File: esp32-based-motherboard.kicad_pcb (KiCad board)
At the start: 2 copper layers, 4 parts, among them J1 HR911105A, U1 ESP32-P4_MODULE, U2 LAN8720A, U3 ADM3053

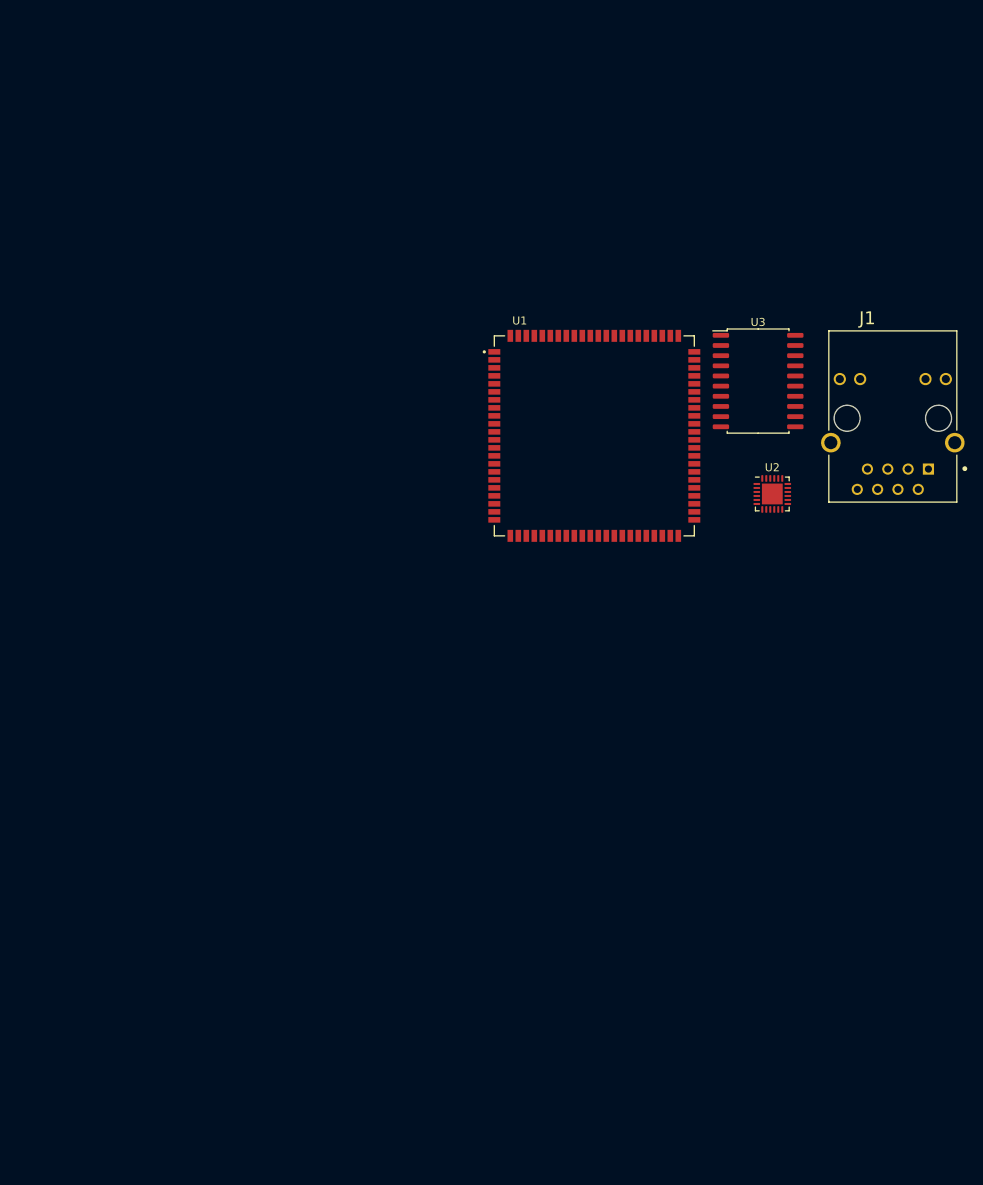
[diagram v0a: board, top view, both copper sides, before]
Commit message: ESP32 P4 with 8 Ethernet
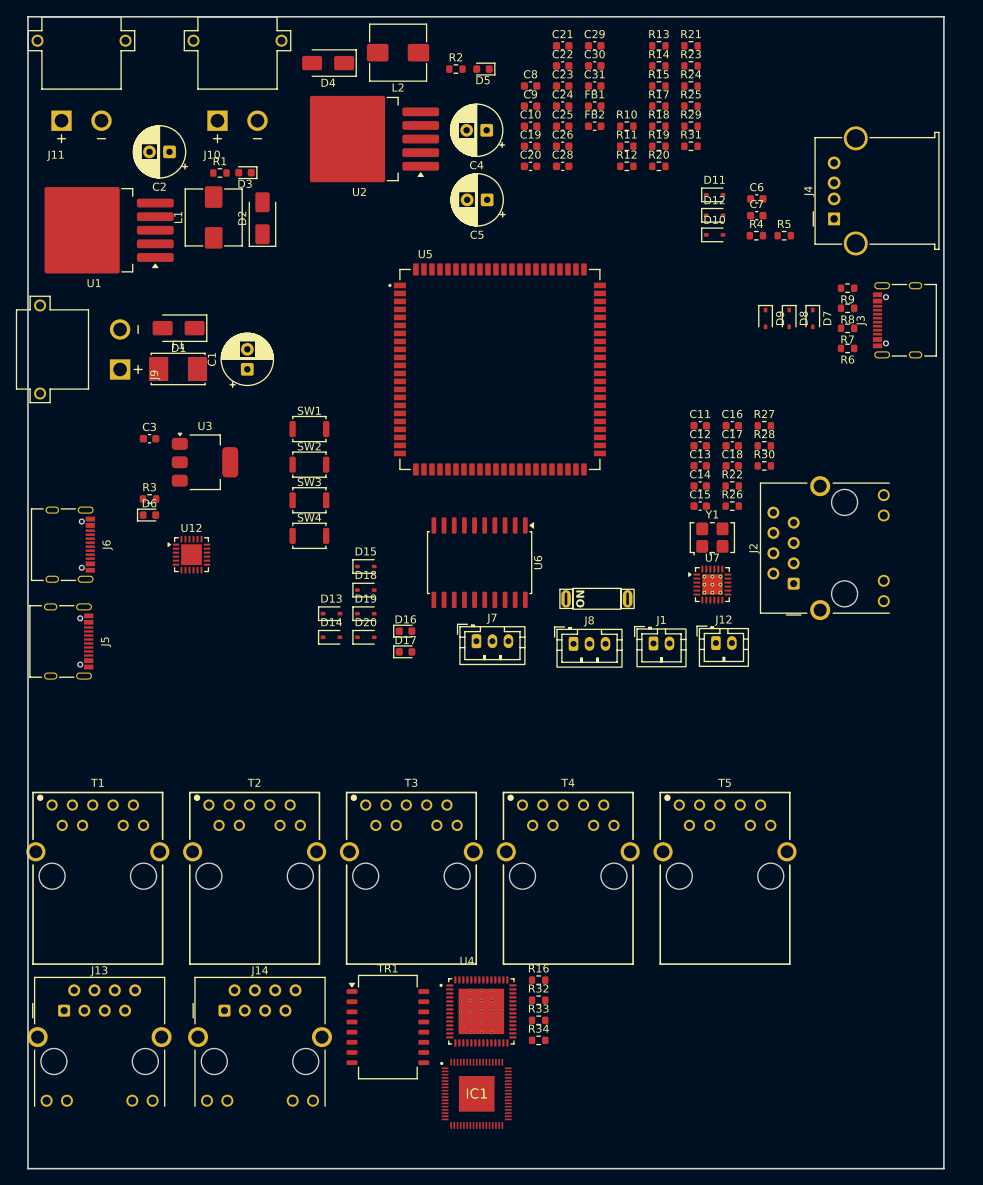
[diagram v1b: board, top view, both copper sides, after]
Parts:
- added C1: 470UF, Capacitor_THT:CP_Radial_D6.3mm_P2.50mm, F.Cu at (64.1, 62.3)
- added C10: 0.1uF, Capacitor_SMD:C_0603_1608Metric, F.Cu at (99.5, 31.9)
- added C11: 10uF, Capacitor_SMD:C_0603_1608Metric, F.Cu at (120.7, 69.3)
- added C12: 0.1uF, Capacitor_SMD:C_0603_1608Metric, F.Cu at (120.7, 71.8)
- added C13: 0.1uF, Capacitor_SMD:C_0603_1608Metric, F.Cu at (120.7, 74.4)
- added C14: 0.1uF, Capacitor_SMD:C_0603_1608Metric, F.Cu at (120.7, 76.9)
- added C15: 470pF, Capacitor_SMD:C_0603_1608Metric, F.Cu at (120.7, 79.4)
- added C16: 1uF, Capacitor_SMD:C_0603_1608Metric, F.Cu at (124.7, 69.3)
- added C17: 12pF, Capacitor_SMD:C_0603_1608Metric, F.Cu at (124.7, 71.8)
- added C18: 12pF, Capacitor_SMD:C_0603_1608Metric, F.Cu at (124.7, 74.4)
- added C19: 0.1uF, Capacitor_SMD:C_0603_1608Metric, F.Cu at (99.5, 34.4)
- added C2: 47UF, Capacitor_THT:CP_Radial_D6.3mm_P2.50mm, F.Cu at (54.4, 35.1)
- added C20: 10uF, Capacitor_SMD:C_0603_1608Metric, F.Cu at (99.5, 36.9)
- added C21: 0.01uF, Capacitor_SMD:C_0603_1608Metric, F.Cu at (103.5, 21.9)
- added C22: 0.1uF, Capacitor_SMD:C_0603_1608Metric, F.Cu at (103.5, 24.4)
- added C23: 10uF, Capacitor_SMD:C_0603_1608Metric, F.Cu at (103.5, 26.9)
- added C24: 10nF, Capacitor_SMD:C_0603_1608Metric, F.Cu at (103.5, 29.4)
- added C25: 100nF, Capacitor_SMD:C_0603_1608Metric, F.Cu at (103.5, 31.9)
- added C26: 0.1uF, Capacitor_SMD:C_0603_1608Metric, F.Cu at (103.5, 34.4)
- added C28: 10uF, Capacitor_SMD:C_0603_1608Metric, F.Cu at (103.5, 36.9)
- added C29: 0.1uF, Capacitor_SMD:C_0603_1608Metric, F.Cu at (107.6, 21.9)
- added C3: 10uF, Capacitor_SMD:C_0603_1608Metric, F.Cu at (51.9, 71.0)
- added C30: 0.1uF, Capacitor_SMD:C_0603_1608Metric, F.Cu at (107.6, 24.4)
- added C31: 10uF, Capacitor_SMD:C_0603_1608Metric, F.Cu at (107.6, 26.9)
- added C4: 470UF, Capacitor_THT:CP_Radial_D6.3mm_P2.50mm, F.Cu at (94.0, 32.4)
- added C5: 47UF, Capacitor_THT:CP_Radial_D6.3mm_P2.50mm, F.Cu at (94.1, 41.1)
- added C6: 10uF, Capacitor_SMD:C_0603_1608Metric, F.Cu at (127.8, 41.0)
- added C7: 0.1uF, Capacitor_SMD:C_0603_1608Metric, F.Cu at (127.8, 43.1)
- added C8: 0.1uF, Capacitor_SMD:C_0603_1608Metric, F.Cu at (99.5, 26.9)
- added C9: 10uF, Capacitor_SMD:C_0603_1608Metric, F.Cu at (99.5, 29.4)
- added D1: SS56, Diode_SMD:D_SMA, F.Cu at (55.5, 57.1)
- added D10: SD05C-01F, Diode_SMD:D_SOD-323, F.Cu at (122.5, 45.5)
- added D11: SD05C-01F, Diode_SMD:D_SOD-323, F.Cu at (122.5, 40.5)
- added D12: SD05C-01F, Diode_SMD:D_SOD-323, F.Cu at (122.5, 43.0)
- added D13: SD05C-01F, Diode_SMD:D_SOD-323, F.Cu at (74.6, 92.8)
- added D14: SD05C-01F, Diode_SMD:D_SOD-323, F.Cu at (74.6, 95.8)
- added D15: SD05C-01F, Diode_SMD:D_SOD-323, F.Cu at (78.9, 86.9)
- added D16: LED, LED_SMD:LED_0603_1608Metric, F.Cu at (83.9, 95.0)
- added D17: LED, LED_SMD:LED_0603_1608Metric, F.Cu at (83.9, 97.6)
- added D18: SD05C-01F, Diode_SMD:D_SOD-323, F.Cu at (78.9, 89.9)
- added D19: SD05C-01F, Diode_SMD:D_SOD-323, F.Cu at (78.9, 92.8)
- added D2: 1N5822, Diode_SMD:D_SMA, F.Cu at (66.0, 43.4)
- added D20: SD05C-01F, Diode_SMD:D_SOD-323, F.Cu at (78.9, 95.8)
- added D3: LED, LED_SMD:LED_0603_1608Metric, F.Cu at (63.8, 37.7)
- added D4: 1N5822, Diode_SMD:D_SMA, F.Cu at (74.2, 24.0)
- added D5: LED, LED_SMD:LED_0603_1608Metric, F.Cu at (93.6, 24.8)
- added D6: LED, LED_SMD:LED_0603_1608Metric, F.Cu at (51.9, 80.5)
- added D7: ESD7951ST5G, Diode_SMD:D_SOD-323, F.Cu at (134.8, 55.9)
- added D8: ESD7951ST5G, Diode_SMD:D_SOD-323, F.Cu at (131.9, 55.9)
- added D9: SD05C-01F, Diode_SMD:D_SOD-323, F.Cu at (128.9, 55.9)
- added F1: Fuse, Fuse:Fuseholder_Littelfuse_Nano2_157x, F.Cu at (55.5, 62.2)
- added FB1: FerriteBead, Inductor_SMD:L_0603_1608Metric, F.Cu at (107.6, 29.4)
- added FB2: FerriteBead, Inductor_SMD:L_0603_1608Metric, F.Cu at (107.6, 31.9)
- added IC1: IP178GI, Custom_Footprint:IP178GI, F.Cu at (92.8, 152.8)
- added J10: XT30PW-M, Custom_Footprint:AMASS_XT30PW-M, F.Cu at (62.9, 21.2)
- added J11: XT30PW-M, Custom_Footprint:AMASS_XT30PW-M, F.Cu at (43.4, 21.2)
- added J12: Conn_01x02_Pin, Connector_JST:JST_PH_B2B-PH-K_1x02_P2.00mm_Vertical, F.Cu at (122.7, 96.5)
- added J13: RJ45_Hanrun_HR911105A_Horizontal, Connector_RJ:RJ45_Hanrun_HR911105A_Horizontal, F.Cu at (41.2, 142.4)
- added J14: RJ45_Hanrun_HR911105A_Horizontal, Connector_RJ:RJ45_Hanrun_HR911105A_Horizontal, F.Cu at (61.3, 142.4)
- added J2: RJ45_Hanrun_HR911105A_Horizontal, Connector_RJ:RJ45_Hanrun_HR911105A_Horizontal, F.Cu at (132.4, 89.1)
- added J3: USB_C_Receptacle_USB2.0_16P, Connector_USB:USB_C_Receptacle_Palconn_UTC16-G, F.Cu at (145.4, 56.1)
- added J4: USB_A, Connector_USB:USB_A_Molex_67643_Horizontal, F.Cu at (137.5, 43.5)
- added J5: USB_C_Receptacle_USB2.0_16P, Connector_USB:USB_C_Receptacle_Palconn_UTC16-G, F.Cu at (41.8, 96.3)
- added J6: USB_C_Receptacle_USB2.0_16P, Connector_USB:USB_C_Receptacle_Palconn_UTC16-G, F.Cu at (42.0, 84.2)
- added J7: Conn_01x03_Pin, Connector_JST:JST_PH_B3B-PH-K_1x03_P2.00mm_Vertical, F.Cu at (92.8, 96.3)
- added J8: Conn_01x03_Pin, Connector_JST:JST_PH_B3B-PH-K_1x03_P2.00mm_Vertical, F.Cu at (104.9, 96.6)
- added J9: XT30PW-M, Custom_Footprint:AMASS_XT30PW-M, F.Cu at (38.2, 59.8)
- added L1: 47uH, Inductor_SMD:L_Wuerth_HCI-7030, F.Cu at (59.9, 43.3)
- added L2: 47uH, Inductor_SMD:L_Wuerth_HCI-7030, F.Cu at (83.0, 22.7)
- added R1: 2k, Resistor_SMD:R_0603_1608Metric, F.Cu at (60.7, 37.7)
- added R10: 10k, Resistor_SMD:R_0603_1608Metric, F.Cu at (111.6, 31.9)
- added R11: 10k, Resistor_SMD:R_0603_1608Metric, F.Cu at (111.6, 34.4)
- added R12: 5.1k, Resistor_SMD:R_0603_1608Metric, F.Cu at (111.6, 36.9)
- added R13: 10k, Resistor_SMD:R_0603_1608Metric, F.Cu at (115.6, 21.9)
- added R14: 5.1k, Resistor_SMD:R_0603_1608Metric, F.Cu at (115.6, 24.4)
- added R15: 10k, Resistor_SMD:R_0603_1608Metric, F.Cu at (115.6, 26.9)
- added R16: 500, Resistor_SMD:R_0603_1608Metric, F.Cu at (100.5, 138.6)
- added R17: 5.1k, Resistor_SMD:R_0603_1608Metric, F.Cu at (115.6, 29.4)
- added R18: 5.1k, Resistor_SMD:R_0603_1608Metric, F.Cu at (115.6, 31.9)
- added R19: 47k, Resistor_SMD:R_0603_1608Metric, F.Cu at (115.6, 34.4)
- added R2: 1k, Resistor_SMD:R_0603_1608Metric, F.Cu at (90.2, 24.8)
- added R20: 1k, Resistor_SMD:R_0603_1608Metric, F.Cu at (115.6, 36.9)
- added R21: 10k, Resistor_SMD:R_0603_1608Metric, F.Cu at (119.6, 21.9)
- added R22: 500, Resistor_SMD:R_0603_1608Metric, F.Cu at (124.7, 76.9)
- added R23: 1k, Resistor_SMD:R_0603_1608Metric, F.Cu at (119.6, 24.4)
- added R24: 0, Resistor_SMD:R_0603_1608Metric, F.Cu at (119.6, 26.9)
- added R25: 120, Resistor_SMD:R_0603_1608Metric, F.Cu at (119.6, 29.4)
- added R26: 10k, Resistor_SMD:R_0603_1608Metric, F.Cu at (124.7, 79.4)
- added R27: 10k, Resistor_SMD:R_0603_1608Metric, F.Cu at (128.8, 69.3)
- added R28: 12.1k (1%), Resistor_SMD:R_0603_1608Metric, F.Cu at (128.8, 71.8)
- added R29: 10k, Resistor_SMD:R_0603_1608Metric, F.Cu at (119.6, 31.9)
- added R3: 500, Resistor_SMD:R_0603_1608Metric, F.Cu at (51.9, 78.5)
- added R30: 500, Resistor_SMD:R_0603_1608Metric, F.Cu at (128.8, 74.4)
- added R31: 1k, Resistor_SMD:R_0603_1608Metric, F.Cu at (119.6, 34.4)
- added R32: 500, Resistor_SMD:R_0603_1608Metric, F.Cu at (100.5, 141.1)
- added R33: 500, Resistor_SMD:R_0603_1608Metric, F.Cu at (100.5, 143.7)
- added R34: 500, Resistor_SMD:R_0603_1608Metric, F.Cu at (100.5, 146.2)
- added R4: 0, Resistor_SMD:R_0603_1608Metric, F.Cu at (127.8, 45.6)
- added R5: 0, Resistor_SMD:R_0603_1608Metric, F.Cu at (131.2, 45.6)
- added R6: 0, Resistor_SMD:R_0603_1608Metric, F.Cu at (139.2, 59.7)
- added R7: 0, Resistor_SMD:R_0603_1608Metric, F.Cu at (139.2, 57.2)
- added R8: 5.1k, Resistor_SMD:R_0603_1608Metric, F.Cu at (139.2, 54.6)
- added R9: 5.1k, Resistor_SMD:R_0603_1608Metric, F.Cu at (139.2, 52.1)
- added SW1: SW_Push, Button_Switch_SMD:SW_Push_SPST_NO_Alps_SKRK, F.Cu at (71.9, 69.8)
- added SW2: SW_Push, Button_Switch_SMD:SW_Push_SPST_NO_Alps_SKRK, F.Cu at (71.9, 74.2)
- added SW3: SW_Push, Button_Switch_SMD:SW_Push_SPST_NO_Alps_SKRK, F.Cu at (71.9, 78.7)
- added SW4: SW_Push, Button_Switch_SMD:SW_Push_SPST_NO_Alps_SKRK, F.Cu at (71.9, 83.1)
- added SW5: SW_SPST, Custom_Footprint:DSIC01LHGET_C54957, F.Cu at (108.3, 89.7)
- added T1: WE-RJ45_7499211002A, Custom_Footprint:WE-RJ45_7499211002A, F.Cu at (45.4, 125.6)
- added T2: WE-RJ45_7499211002A, Custom_Footprint:WE-RJ45_7499211002A, F.Cu at (65.0, 125.6)
- added T3: WE-RJ45_7499211002A, Custom_Footprint:WE-RJ45_7499211002A, F.Cu at (84.6, 125.6)
- added T4: WE-RJ45_7499211002A, Custom_Footprint:WE-RJ45_7499211002A, F.Cu at (104.2, 125.6)
- added T5: WE-RJ45_7499211002A, Custom_Footprint:WE-RJ45_7499211002A, F.Cu at (123.8, 125.6)
- added TR1: TG110-S050N2xx, Transformer_SMD:Transformer_Ethernet_Halo_N2_SO-16_7.11x12.7mm, F.Cu at (81.7, 144.5)
- added U12: CP2102N-Axx-xQFN24, Package_DFN_QFN:QFN-24-1EP_4x4mm_P0.5mm_EP2.6x2.6mm, F.Cu at (57.1, 85.5)
- added U4: TPS23880RTQT, Custom_Footprint:TPS23880RTQT, F.Cu at (93.4, 142.5)
- added U5: ESP32-P4_MODULE, Custom_Footprint:ESP32-P4_MODULE, F.Cu at (95.7, 62.3)
- added U6: ADM3053, Package_SO:SOIC-20W_7.5x12.8mm_P1.27mm, F.Cu at (93.2, 86.5)
- added U7: LAN8720A, Package_DFN_QFN:VQFN-24-1EP_4x4mm_P0.5mm_EP2.5x2.5mm_ThermalVias, F.Cu at (122.3, 89.2)
- added Y1: 25MHz, Oscillator:Oscillator_SMD_SiT_PQFN-4Pin_5.0x3.2mm, F.Cu at (122.3, 83.3)
- J1: value HR911105A -> Conn_01x02_Pin; footprint Connector_RJ:HANRUN_HR911105A -> Connector_JST:JST_PH_B2B-PH-K_1x02_P2.00mm_Vertical
- U1: value ESP32-P4_MODULE -> LM2596S-12; footprint ESP32-P4:XCVR_ESP32-P4_MODULE -> Package_TO_SOT_SMD:TO-263-5_TabPin3
- U2: value LAN8720A -> LM2596S-5; footprint Package_DFN_QFN:QFN-24-1EP_4x4mm_P0.5mm_EP2.6x2.6mm -> Package_TO_SOT_SMD:TO-263-5_TabPin3
- U3: value ADM3053 -> AMS1117-3.3; footprint Package_SO:SOIC-20W_7.5x12.8mm_P1.27mm -> Package_TO_SOT_SMD:SOT-223-3_TabPin2
- moved U3 69.9 mm to (58.8, 73.9)
- moved U2 68.0 mm to (78.2, 33.5), turned to 180 degrees
- moved U1 67.6 mm to (45.0, 44.9), turned to 180 degrees
- moved J1 41.1 mm to (114.9, 96.5)
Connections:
- J1 pad 1: unconnected-(J1-Pad1) -> +5V
- J1 pad 2: unconnected-(J1-Pad2) -> GND
- U1 pad 1: GND -> /power_system/Vcc
- U1 pad 2: unconnected-(U1-LNA_OUT-Pad2) -> Net-(D2-K)
- U1 pad 4: unconnected-(U1-C6_U0RXD-Pad4) -> +12V
- U1 pad 5: unconnected-(U1-C6_U0TXD-Pad5) -> GND
- U2 pad 1: unconnected-(U2-VDD2A-Pad1) -> /power_system/Vcc
- U2 pad 2: unconnected-(U2-LED2/nINTSEL-Pad2) -> Net-(D4-K)
- U2 pad 3: unconnected-(U2-LED1/REGOFF-Pad3) -> GND
- U2 pad 4: unconnected-(U2-XTAL2-Pad4) -> +5V
- U2 pad 5: unconnected-(U2-XTAL1/CLKIN-Pad5) -> GND
- U3 pad 1: unconnected-(U3-GND1-Pad1) -> GND
- U3 pad 2: unconnected-(U3-NC-Pad2) -> +3.3V
- U3 pad 3: unconnected-(U3-GND1-Pad3) -> +5V
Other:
- board outline added: 114.5 x 144 mm
